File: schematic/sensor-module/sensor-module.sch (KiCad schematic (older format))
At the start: 18 parts, among them K1 SENSORS, K2 LEDs, K3 SENSORS, K4 LEDs, P1 Vibro, P2 VibroEngine, P3 Vibro, U1 RGB-LED, U2 RGB-LED

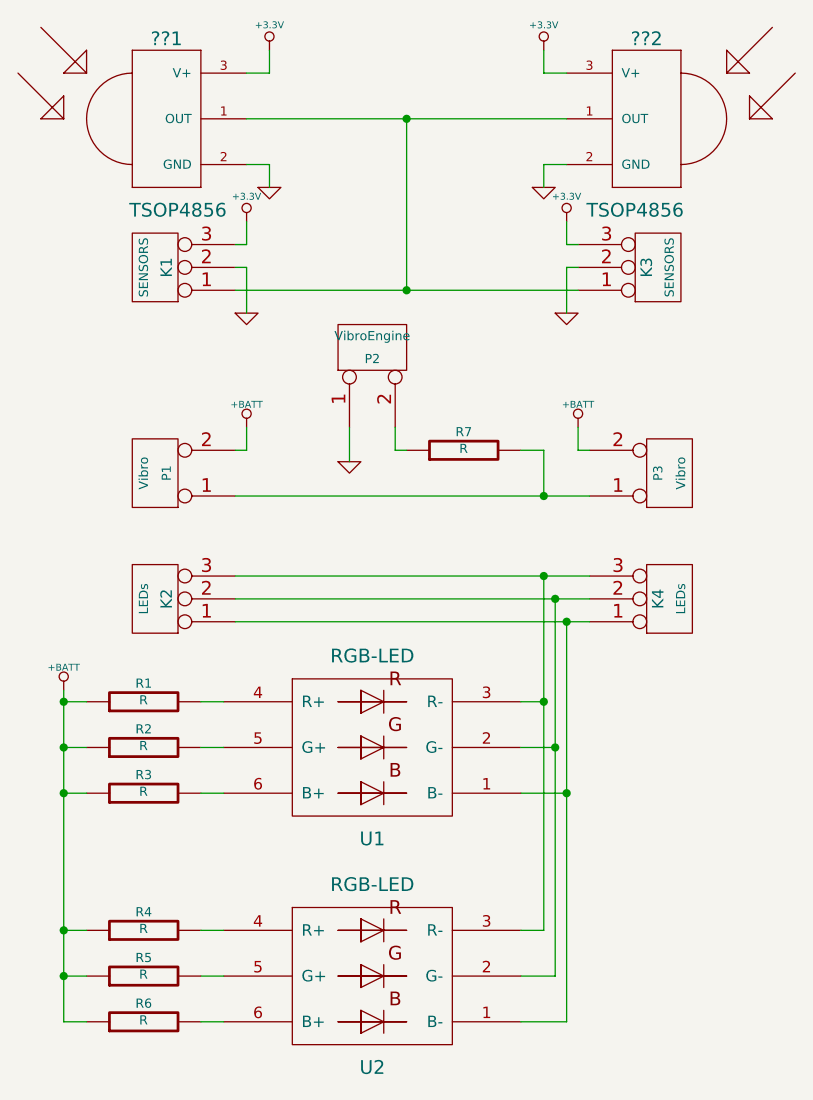
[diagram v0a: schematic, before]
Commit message: sensor module pcb fixed for vibroengine
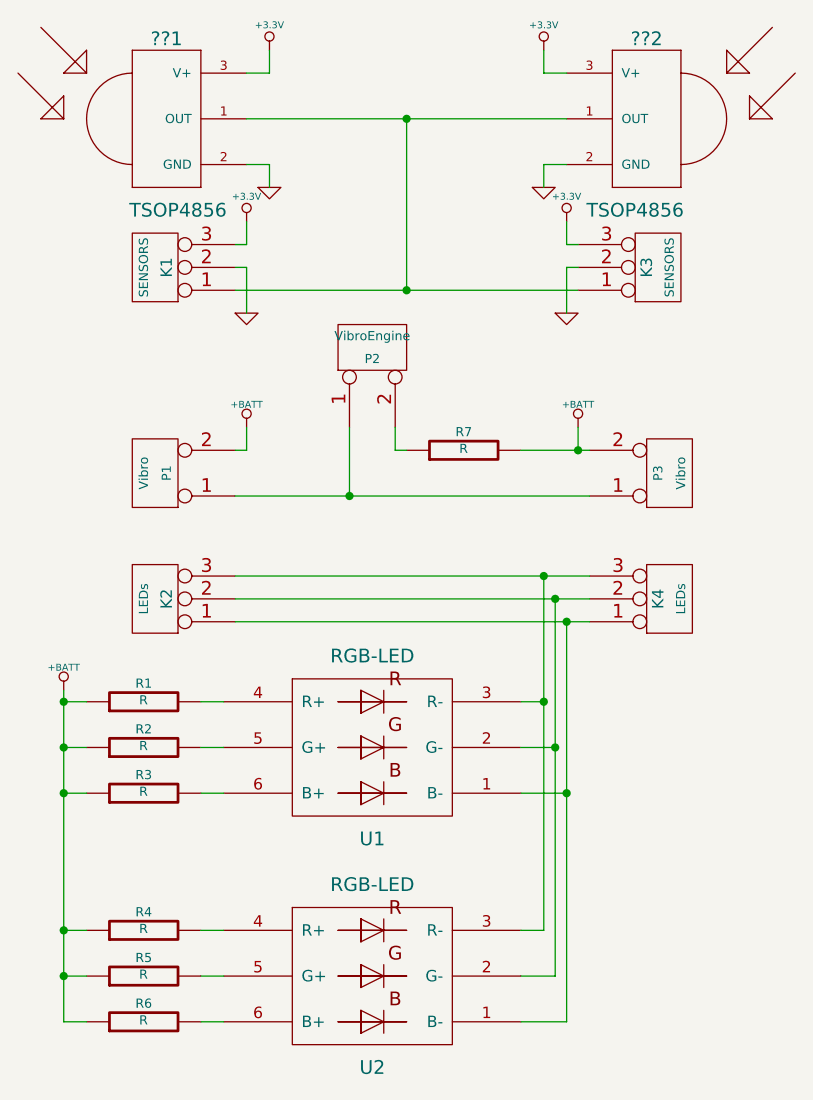
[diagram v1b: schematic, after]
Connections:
- net +BATT: now also R7.2
- net GND: no longer P2.1 (P1)
- net at P1.1 (P1), P3.1 (P1): now also P2.1 (P1); no longer R7.2
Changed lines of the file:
@@
 LIBS:contrib
 LIBS:valves
-LIBS:tsop4856
 LIBS:led_rgb
 LIBS:led
-LIBS:rgb-led
 LIBS:sensor-module-cache
 EELAYER 27 0
@@
 encoding utf-8
 Sheet 1 1
-Title ""
-Date "29 mar 2015"
-Rev ""
+Title "Sensor module"
+Date "21 apr 2015"
+Rev "1"
 Comp ""
 Comment1 ""
@@
 	1    0    0    -1
 $EndComp
-$Comp
-L GND #PWR010
-U 1 1 5517BBAF
-P 3800 3800
-F 0 "#PWR010" H 3800 3800 30  0001 C CNN
-F 1 "GND" H 3800 3730 30  0001 C CNN
-F 2 "" H 3800 3800 60  0000 C CNN
-F 3 "" H 3800 3800 60  0000 C CNN
-	1    3800 3800
-	1    0    0    -1
-$EndComp
 Wire Wire Line
 	3350 2100 3450 2100
@@
 	3350 3750 3350 3650
 Wire Wire Line
-	3800 3650 3800 3800
+	3800 3650 3800 3950
 Wire Wire Line
 	4000 3650 4000 3750
@@
 	3300 3950 4850 3950
 Wire Wire Line
-	4650 3950 4650 3750
-Wire Wire Line
-	4650 3750 4550 3750
+	4550 3750 4850 3750
 $Comp
 L CONN_2 P3
@@
 	1    0    0    1
 $EndComp
-Connection ~ 4650 3950
-$Comp
-L +BATT #PWR011
+$Comp
+L +BATT #PWR010
 U 1 1 5517BC65
 P 4800 3650
-F 0 "#PWR011" H 4800 3600 20  0001 C CNN
+F 0 "#PWR010" H 4800 3600 20  0001 C CNN
 F 1 "+BATT" H 4800 3750 30  0000 C CNN
 F 2 "" H 4800 3650 60  0000 C CNN
@@
 $EndComp
 Wire Wire Line
-	4800 3650 4800 3750
-Wire Wire Line
-	4800 3750 4850 3750
+	4800 3750 4800 3650
 $Comp
 L CONN_3 K2
@@
 	3150 5250 3250 5250
 $Comp
-L +BATT #PWR012
+L +BATT #PWR011
 U 1 1 5517C042
 P 2550 4800
-F 0 "#PWR012" H 2550 4750 20  0001 C CNN
+F 0 "#PWR011" H 2550 4750 20  0001 C CNN
 F 1 "+BATT" H 2550 4900 30  0000 C CNN
 F 2 "" H 2550 4800 60  0000 C CNN
@@
 	4050 2300 4050 3050
 Connection ~ 4050 3050
+Connection ~ 4800 3750
+Connection ~ 3800 3950
 $EndSCHEMATC
